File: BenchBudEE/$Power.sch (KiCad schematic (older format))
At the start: 11 parts, among them P1 CONN_12X2, SW1 SWITCH_INV

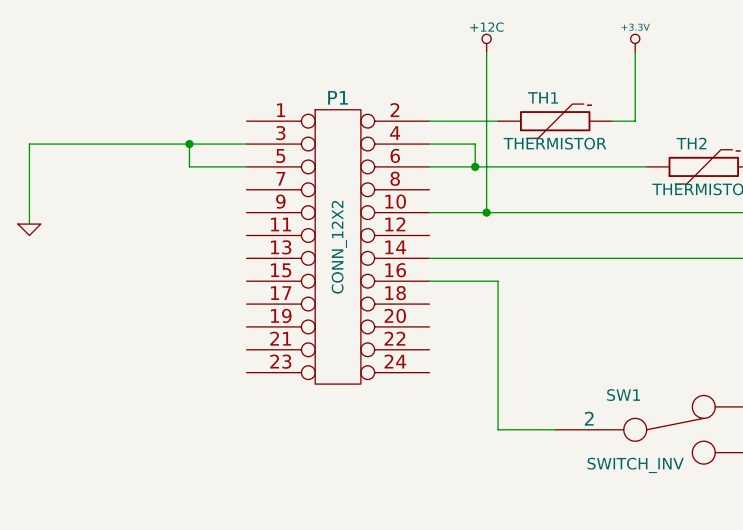
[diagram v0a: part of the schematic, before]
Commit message: Connectors added + associated + roughly placed.
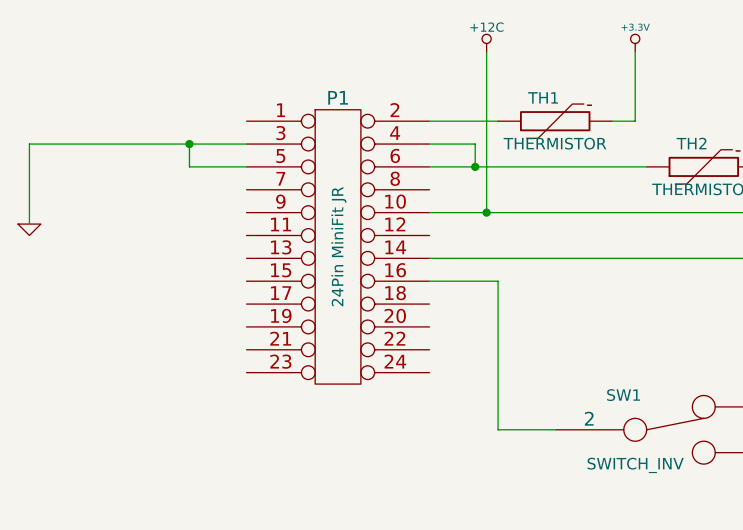
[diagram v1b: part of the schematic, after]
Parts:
- P1: value CONN_12X2 -> 24Pin MiniFit JR; Distributor (none) -> Mouser; Distributor Part Link (none) -> http://uk.mouser.com/ProductDetail/Molex/39-30-1240/?qs=sGA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; Distributor Part Number (none) -> 538-39-30-1240; MFG Name (none) -> Molex; MFG Part Number (none) -> 39-30-1240
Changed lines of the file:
@@
 Sheet 5 9
 Title ""
-Date "20 feb 2014"
+Date "21 feb 2014"
 Rev ""
 Comp ""
@@
 P 3000 2300
 F 0 "P1" H 3000 2950 60  0000 C CNN
-F 1 "CONN_12X2" V 3000 2300 50  0000 C CNN
+F 1 "24Pin MiniFit JR" V 3000 2300 50  0000 C CNN
 F 2 "" H 3000 2300 60  0000 C CNN
-F 3 "" H 3000 2300 60  0000 C CNN
+F 3 "http://www.molex.com/webdocs/datasheets/pdf/en-us/0039301240_PCB_HEADERS.pdf" H 3000 2300 60  0001 C CNN
+F 4 "Molex" H 3000 2300 60  0001 C CNN "MFG Name"
+F 5 "39-30-1240" H 3000 2300 60  0001 C CNN "MFG Part Number"
+F 6 "Mouser" H 3000 2300 60  0001 C CNN "Distributor"
+F 7 "538-39-30-1240" H 3000 2300 60  0001 C CNN "Distributor Part Number"
+F 8 "http://uk.mouser.com/ProductDetail/Molex/39-30-1240/?qs=sGAEpiMZZMs%252bGHln7q6pm%252bS0pk2Wo0Xxrf8ldfSZpwQ=" H 3000 2300 60  0001 C CNN "Distributor Part Link"
 	1    3000 2300
 	1    0    0    -1
@@
 	1650 1850 1650 2200
 $Comp
-L GND #PWR010
+L GND #PWR10
 U 1 1 52F2DAF8
 P 1650 2200
-F 0 "#PWR010" H 1650 2200 30  0001 C CNN
+F 0 "#PWR10" H 1650 2200 30  0001 C CNN
 F 1 "GND" H 1650 2130 30  0001 C CNN
 F 2 "" H 1650 2200 60  0000 C CNN
@@
 $EndComp
 $Comp
-L +3.3V #PWR011
+L +3.3V #PWR12
 U 1 1 52F2DB2F
 P 4300 1450
-F 0 "#PWR011" H 4300 1410 30  0001 C CNN
+F 0 "#PWR12" H 4300 1410 30  0001 C CNN
 F 1 "+3.3V" H 4300 1560 30  0000 C CNN
 F 2 "" H 4300 1450 60  0000 C CNN
@@
 $EndComp
 $Comp
-L +5V #PWR012
+L +5V #PWR13
 U 1 1 52F2DB50
 P 5000 1450
-F 0 "#PWR012" H 5000 1540 20  0001 C CNN
+F 0 "#PWR13" H 5000 1540 20  0001 C CNN
 F 1 "+5V" H 5000 1540 30  0000 C CNN
 F 2 "" H 5000 1450 60  0000 C CNN
@@
 	3600 1850 3400 1850
 $Comp
-L +12P #PWR013
+L +12P #PWR15
 U 1 1 52F2DC76
 P 5700 1450
-F 0 "#PWR013" H 5700 1420 30  0001 C CNN
+F 0 "#PWR15" H 5700 1420 30  0001 C CNN
 F 1 "+12P" H 5700 1550 30  0000 C CNN
 F 2 "" H 5700 1450 60  0000 C CNN
@@
 	5700 2150 5700 1450
 $Comp
-L -12P #PWR014
+L -12P #PWR17
 U 1 1 52F2DCDB
 P 6450 1450
-F 0 "#PWR014" H 6450 1580 20  0001 C CNN
+F 0 "#PWR17" H 6450 1580 20  0001 C CNN
 F 1 "-12P" H 6450 1550 30  0000 C CNN
 F 2 "" H 6450 1450 60  0000 C CNN
@@
 	3700 3100 3950 3100
 $Comp
-L GND #PWR015
+L GND #PWR14
 U 1 1 52F2DD3B
 P 5200 3450
-F 0 "#PWR015" H 5200 3450 30  0001 C CNN
+F 0 "#PWR14" H 5200 3450 30  0001 C CNN
 F 1 "GND" H 5200 3380 30  0001 C CNN
 F 2 "" H 5200 3450 60  0000 C CNN
@@
 $EndComp
 $Comp
-L +3.3V #PWR016
+L +3.3V #PWR16
 U 1 1 52F2DD68
 P 5900 2750
-F 0 "#PWR016" H 5900 2710 30  0001 C CNN
+F 0 "#PWR16" H 5900 2710 30  0001 C CNN
 F 1 "+3.3V" H 5900 2860 30  0000 C CNN
 F 2 "" H 5900 2750 60  0000 C CNN
@@
 	5900 3000 5900 2750
 $Comp
-L +12P #PWR017
+L +12P #PWR18
 U 1 1 52F2DF60
 P 8750 2500
-F 0 "#PWR017" H 8750 2470 30  0001 C CNN
+F 0 "#PWR18" H 8750 2470 30  0001 C CNN
 F 1 "+12P" H 8750 2600 30  0000 C CNN
 F 2 "" H 8750 2500 60  0000 C CNN
@@
 $EndComp
 $Comp
-L -12P #PWR018
+L -12P #PWR19
 U 1 1 52F2DF66
 P 8800 4100
-F 0 "#PWR018" H 8800 4230 20  0001 C CNN
+F 0 "#PWR19" H 8800 4230 20  0001 C CNN
 F 1 "-12P" H 8800 4200 30  0000 C CNN
 F 2 "" H 8800 4100 60  0000 C CNN
@@
 $EndComp
 $Comp
-L GND #PWR019
+L GND #PWR20
 U 1 1 52F2DF6C
 P 9700 3500
-F 0 "#PWR019" H 9700 3500 30  0001 C CNN
+F 0 "#PWR20" H 9700 3500 30  0001 C CNN
 F 1 "GND" H 9700 3430 30  0001 C CNN
 F 2 "" H 9700 3500 60  0000 C CNN
@@
 Connection ~ 10050 3950
 $Comp
-L -12V #PWR020
+L -12V #PWR21
 U 1 1 52F3102F
 P 10300 4100
-F 0 "#PWR020" H 10300 4230 20  0001 C CNN
+F 0 "#PWR21" H 10300 4230 20  0001 C CNN
 F 1 "-12V" H 10300 4200 30  0000 C CNN
 F 2 "" H 10300 4100 60  0000 C CNN
@@
 	10300 3950 10300 4100
 $Comp
-L +12V #PWR021
+L +12V #PWR22
 U 1 1 52F31097
 P 10350 2500
-F 0 "#PWR021" H 10350 2450 20  0001 C CNN
+F 0 "#PWR22" H 10350 2450 20  0001 C CNN
 F 1 "+12V" H 10350 2600 30  0000 C CNN
 F 2 "" H 10350 2500 60  0000 C CNN
@@
 Connection ~ 3650 2150
 $Comp
-L +12C #PWR022
+L +12C #PWR11
 U 1 1 52F7EF09
 P 3650 1450
-F 0 "#PWR022" H 3650 1420 30  0001 C CNN
+F 0 "#PWR11" H 3650 1420 30  0001 C CNN
 F 1 "+12C" H 3650 1560 40  0000 C CNN
 F 2 "" H 3650 1450 60  0000 C CNN
